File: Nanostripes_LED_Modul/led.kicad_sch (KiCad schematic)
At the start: 74 parts, among them Q1 BC 846B, Q2 BC 846B, Q3 BC 846B, Q4 BC 846B, Q5 BC 846B, Q6 BC 846B, Q7 BC 846B, Q8 BC 846B

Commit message: update values
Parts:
- R10, R11, R12, R18, R19, R20, R21, R9: value 120 -> 1k
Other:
- moved on the sheet: D24, D25, D26, D27, D28, D29, D30, D31, D32, D33, D34, D35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

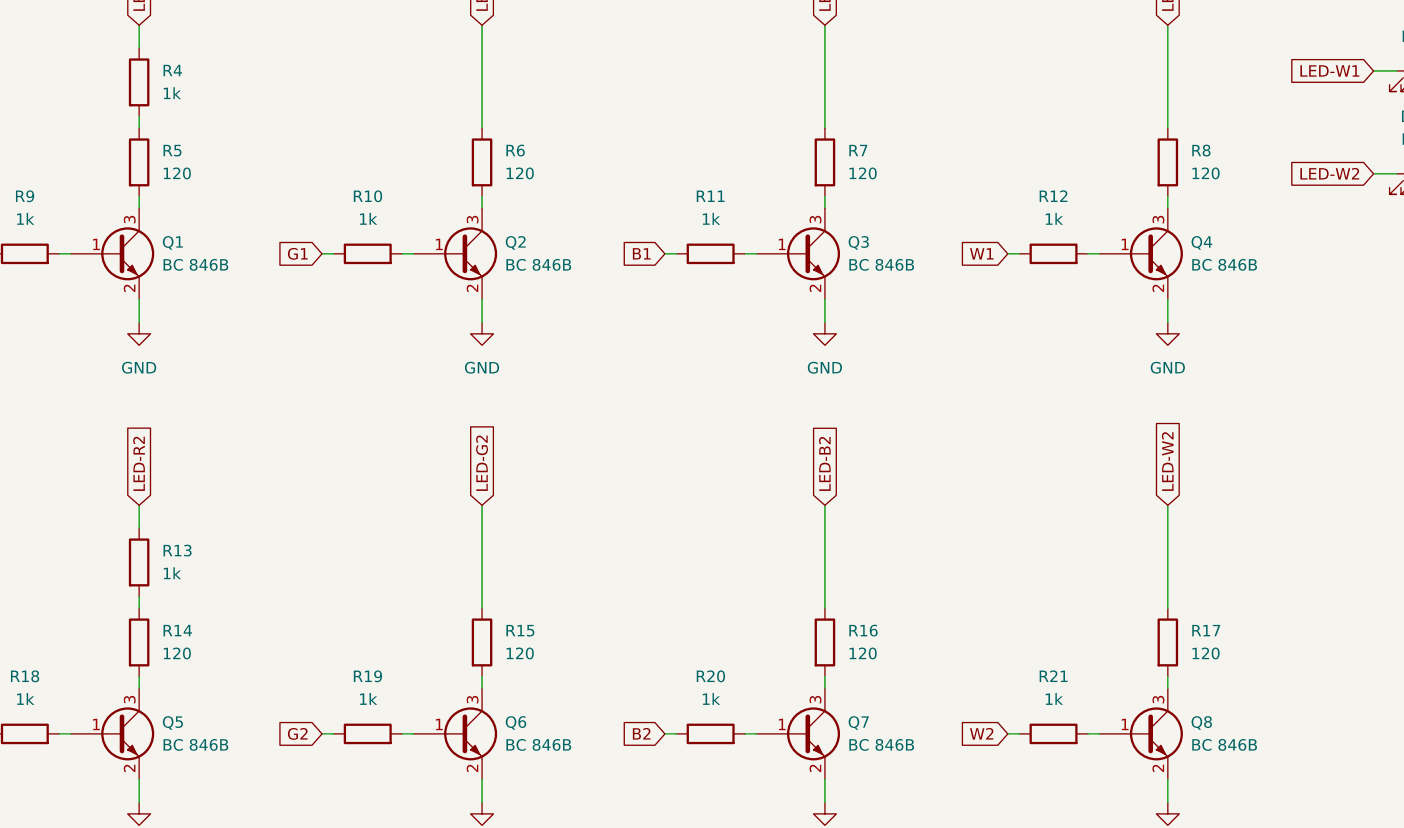
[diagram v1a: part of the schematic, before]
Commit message: updated component values
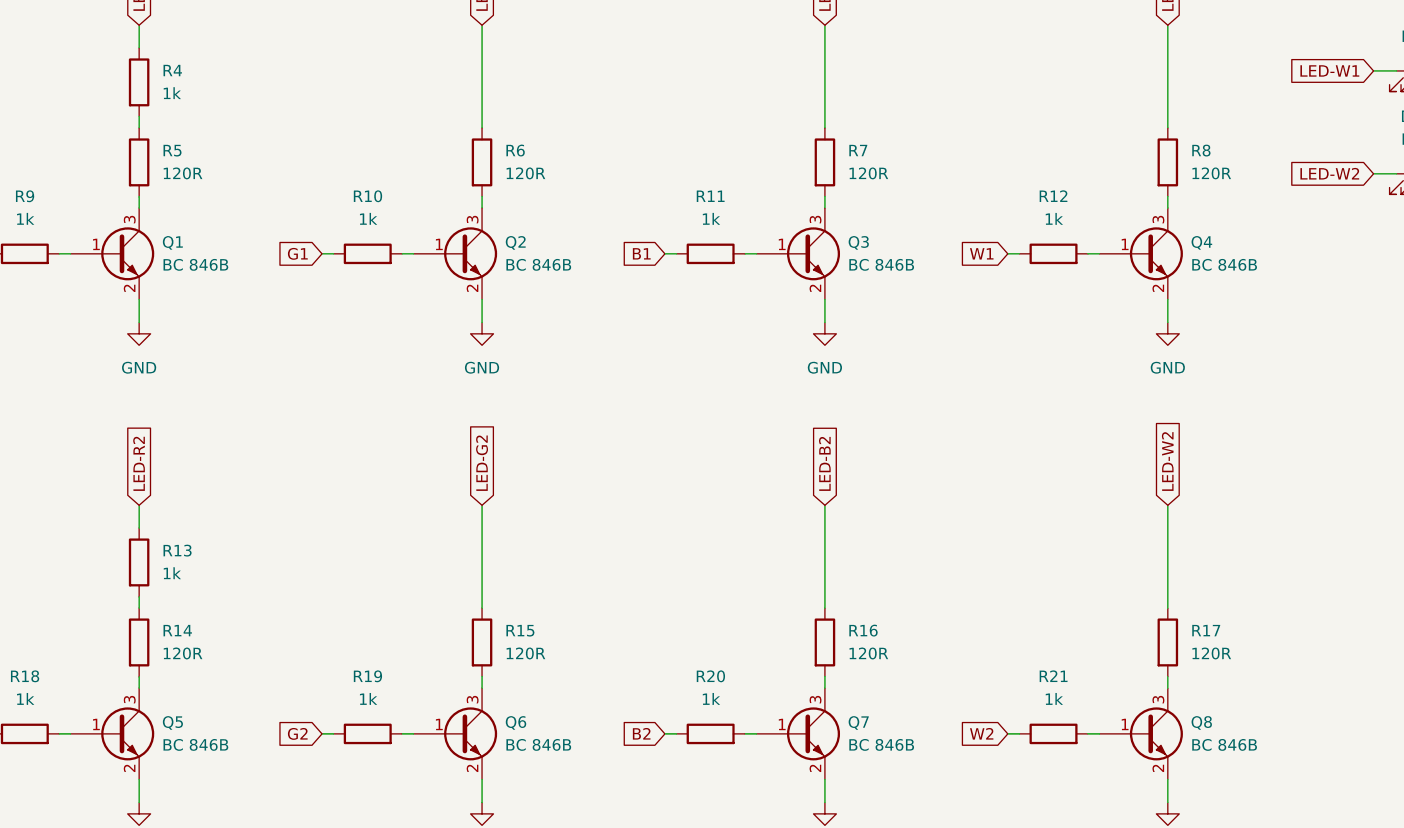
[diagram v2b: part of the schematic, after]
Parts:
- R14, R15, R16, R17, R5, R6, R7, R8: value 120 -> 120R
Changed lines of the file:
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@@
 			)
 		)
-		(property "Value" "120"
+		(property "Value" "120R"
 			(at 114.3 93.9799 0)
 			(effects
@@
 			)
 		)
-		(property "Value" "120"
+		(property "Value" "120R"
 			(at 114.3 40.6399 0)
 			(effects
@@
 			)
 		)
-		(property "Value" "120"
+		(property "Value" "120R"
 			(at 152.4 93.9799 0)
 			(effects
@@
 			)
 		)
-		(property "Value" "120"
+		(property "Value" "120R"
 			(at 38.1 40.6399 0)
 			(effects
@@
 			)
 		)
-		(property "Value" "120"
+		(property "Value" "120R"
 			(at 76.2 93.9799 0)
 			(effects
@@
 			)
 		)
-		(property "Value" "120"
+		(property "Value" "120R"
 			(at 38.1 93.9799 0)
 			(effects
@@
 			)
 		)
-		(property "Value" "120"
+		(property "Value" "120R"
 			(at 76.2 40.6399 0)
 			(effects
@@
 			)
 		)
-		(property "Value" "120"
+		(property "Value" "120R"
 			(at 152.4 40.6399 0)
 			(effects
